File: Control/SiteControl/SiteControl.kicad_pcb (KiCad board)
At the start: 2 copper layers, 109.2 x 48.3 mm, 114 parts, among them J1 RJ50, J2 CONN_01X02, J3 CONN_02X07, J4 CONN_01X06, J5 RS232-Jack, J6 CONN_01X02, J7 USB_A, Q1 BC817-40, Q2 Q_PJFET_GSD, U1 Opto_H11L1M, U10 SS_Relay_VO14642AT, U11 MAX17552, U12 ICL3221, U13 Opto_H11L1M, U14 Opto_H11L1M, U15 12-Bit SPI ADC, U2 Opto_H11L1M, U3 Opto_H11L1M, U4 Opto_H11L1M, U5 Opto_H11L1M, U6 PIC16LF1947, U7 SS_Relay_VO14642AT, U8 SS_Relay_VO14642AT, U9 MC34063, Y1 4MHz

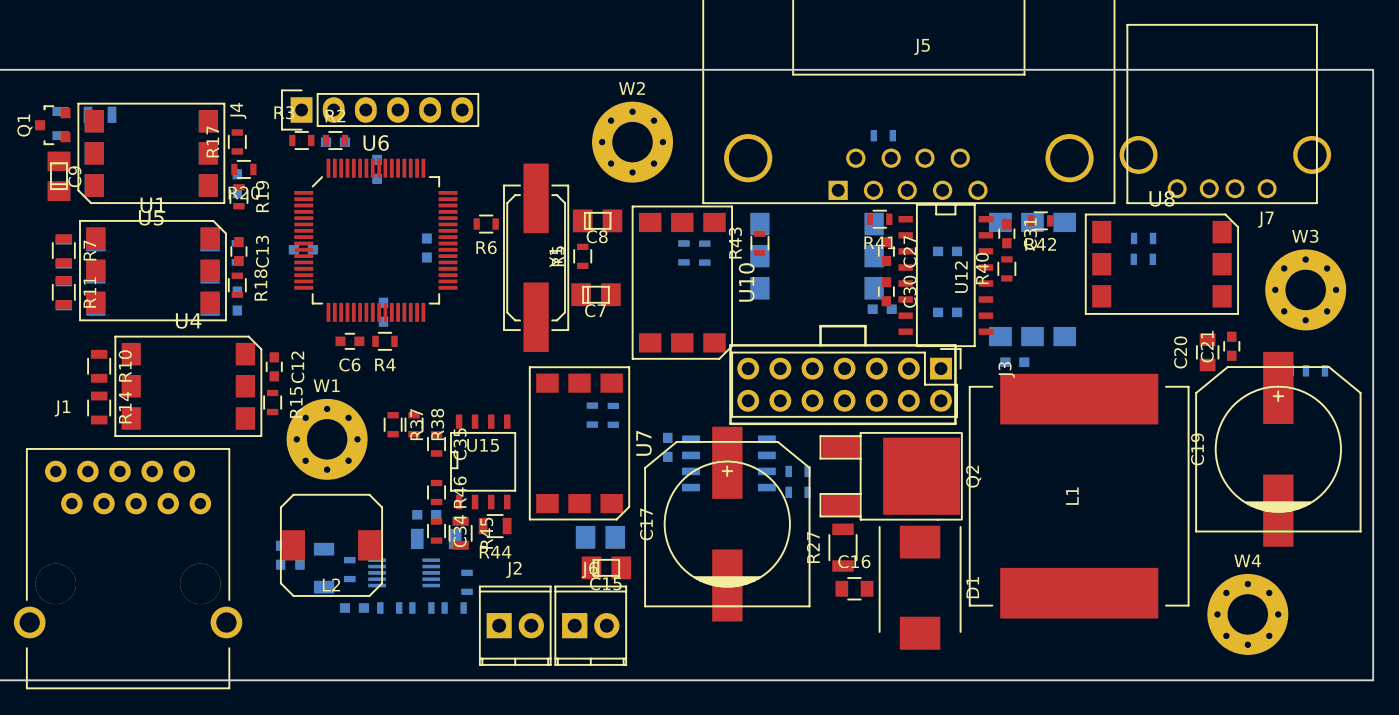
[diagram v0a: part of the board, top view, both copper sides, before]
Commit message: [Changed] Moved mounting holes on control board to positions aligned to 1/16 inch grid
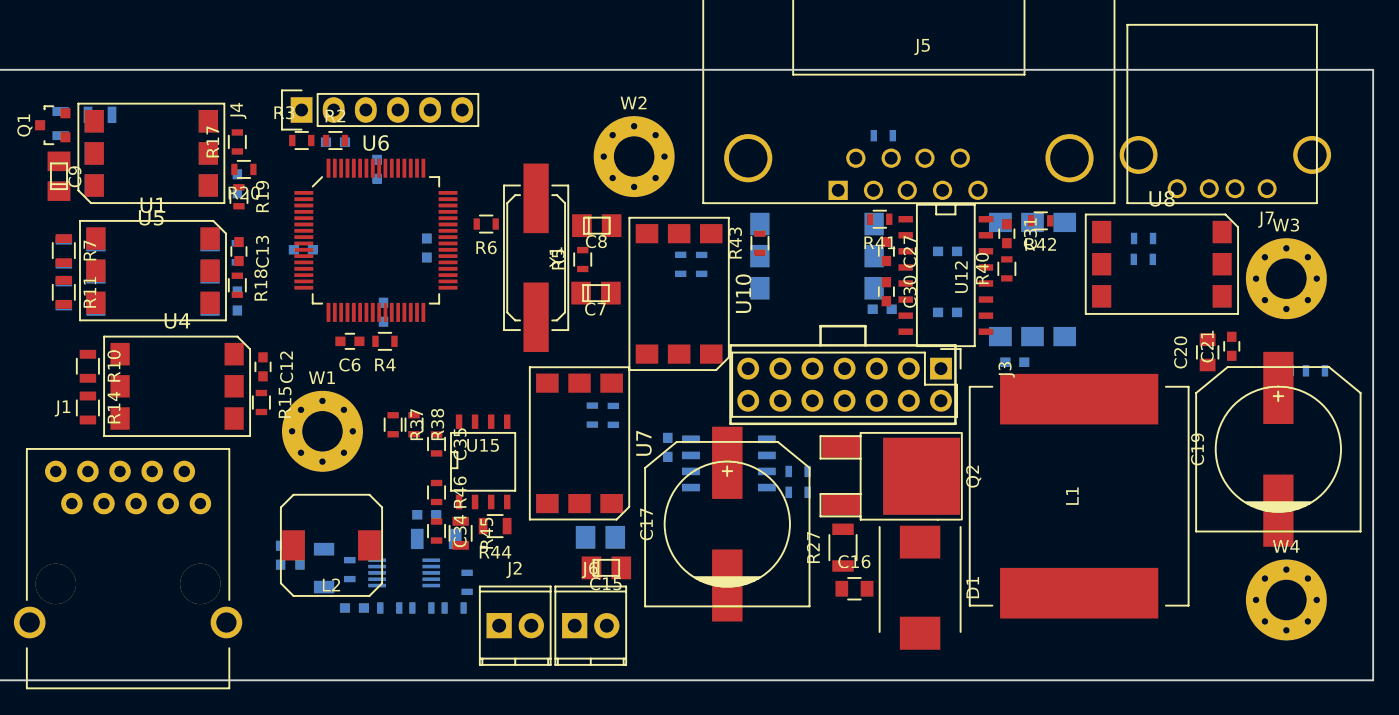
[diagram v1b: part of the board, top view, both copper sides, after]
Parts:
- moved W4 3.26 mm to (188.7, 105.4)
- moved W3 1.76 mm to (188.7, 80.0)
- moved W2 1.15 mm to (137.2, 70.4)
- moved R31 0.92 mm to (140.8, 78.9)
- moved R30 0.92 mm to (142.5, 78.9)
- moved U10 0.92 mm to (140.7, 81.2)
- moved C12 0.89 mm to (107.8, 87.0)
- moved R10 0.89 mm to (94.0, 86.9)
- moved R14 0.89 mm to (94.0, 90.2)
- moved R15 0.89 mm to (107.7, 89.8)
- moved U4 0.89 mm to (101.0, 88.5)
- moved W1 0.73 mm to (112.5, 92.1)
- moved C8 0.39 mm to (134.2, 75.8)
- moved R5 0.25 mm to (133.1, 78.5)
- moved C7 0.13 mm to (134.1, 81.2)
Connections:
- J3 pad 10: CMOS_RTS -> PiSDA
- J3 pad 11: CMOS_RX -> Net-(J3-Pad11)
- J3 pad 12: CMOS_TX -> Pi_VSense
- J3 pad 3: Pi_VSense -> CMOS_TX
- J3 pad 4: Net-(J3-Pad4) -> CMOS_RX
- J3 pad 5: PiSDA -> CMOS_RTS
- J3 pad 6: PiSDA -> CMOS_CTS
- J3 pad 9: CMOS_CTS -> PiSDA
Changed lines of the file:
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@@
     (mod_text_size 1 1)
     (mod_text_width 0.15)
-    (pad_size 1.524 1.524)
-    (pad_drill 0.762)
+    (pad_size 6.4 6.4)
+    (pad_drill 3.2)
     (pad_to_mask_clearance 0.2)
     (aux_axis_origin 0 0)
@@
   (net 115 "Net-(U12-Pad10)")
   (net 116 "Net-(U15-Pad3)")
-  (net 117 "Net-(J4-Pad6)")
-  (net 118 "Net-(J7-Pad3)")
-  (net 119 "Net-(J7-Pad2)")
-  (net 120 "Net-(J7-Pad1)")
-  (net 121 "Net-(J3-Pad4)")
+  (net 117 "Net-(J3-Pad11)")
+  (net 118 "Net-(J4-Pad6)")
+  (net 119 "Net-(J7-Pad3)")
+  (net 120 "Net-(J7-Pad2)")
+  (net 121 "Net-(J7-Pad1)")
   (net_class Default "This is the default net class."
     (clearance 0.2)
@@
     (add_net "Net-(C8-Pad1)")
     (add_net "Net-(D1-Pad1)")
-    (add_net "Net-(J3-Pad4)")
+    (add_net "Net-(J3-Pad11)")
     (add_net "Net-(J4-Pad6)")
     (add_net "Net-(J7-Pad1)")
@@
   )
   (module Capacitors_Tantalum_SMD:TantalC_SizeR_EIA-2012 (layer F.Cu)
-    (at 134.14502 81.28 180)
+    (at 134.14502 81.153 180)
     (descr "Tantal Cap. , Size C, EIA-2012")
     (fp_text reference C7 (at 0.0254 -1.2954 180) (layer F.SilkS)
@@
   )
   (module Capacitors_Tantalum_SMD:TantalC_SizeR_EIA-2012 (layer F.Cu)
-    (at 134.27202 75.438 180)
+    (at 134.20598 75.819 180)
     (descr "Tantal Cap. , Size C, EIA-2012")
     (fp_text reference C8 (at 0.0254 -1.2954 180) (layer F.SilkS)
@@
   )
   (module Resistors_SMD:R_0603 (layer F.Cu)
-    (at 133.096 78.244 90)
+    (at 133.096 78.498 90)
     (descr "Resistor SMD 0603, reflow soldering, Vishay (see dcrcw.pdf)")
     (tags "resistor 0603")
@@
   )
   (module Capacitors_SMD:C_0603 (layer F.Cu)
-    (at 108.712 86.983 270)
+    (at 107.823 86.983 270)
     (descr "Capacitor SMD 0603, reflow soldering, AVX (see smccp.pdf)")
     (tags "capacitor 0603")
@@
   )
   (module Resistors_SMD:R_0805 (layer F.Cu)
-    (at 94.869 86.934 270)
+    (at 93.98 86.934 270)
     (descr "Resistor SMD 0805, reflow soldering, Vishay (see dcrcw.pdf)")
     (tags "resistor 0805")
@@
   )
   (module Resistors_SMD:R_0805 (layer F.Cu)
-    (at 94.869 90.231 270)
+    (at 93.98 90.231 270)
     (descr "Resistor SMD 0805, reflow soldering, Vishay (see dcrcw.pdf)")
     (tags "resistor 0805")
@@
   )
   (module Resistors_SMD:R_0603 (layer F.Cu)
-    (at 108.585 89.801 270)
+    (at 107.696 89.801 270)
     (descr "Resistor SMD 0603, reflow soldering, Vishay (see dcrcw.pdf)")
     (tags "resistor 0603")
@@
   )
   (module Resistors_SMD:R_0603 (layer B.Cu)
-    (at 142.748 77.99 90)
+    (at 142.494 78.879 90)
     (descr "Resistor SMD 0603, reflow soldering, Vishay (see dcrcw.pdf)")
     (tags "resistor 0603")
@@
   )
   (module Resistors_SMD:R_0603 (layer B.Cu)
-    (at 141.097 77.978 90)
+    (at 140.843 78.867 90)
     (descr "Resistor SMD 0603, reflow soldering, Vishay (see dcrcw.pdf)")
     (tags "resistor 0603")
@@
   )
   (module Mounting_Holes:MountingHole_3.2mm_M3_Pad_Via (layer F.Cu)
-    (at 112.89 92.71)
+    (at 112.522 92.075)
     (descr "Mounting Hole 3.2mm, M3")
     (tags "mounting hole 3.2mm m3")
@@
   )
   (module Mounting_Holes:MountingHole_3.2mm_M3_Pad_Via (layer F.Cu)
-    (at 137.033 69.215)
+    (at 137.16 70.358)
     (descr "Mounting Hole 3.2mm, M3")
     (tags "mounting hole 3.2mm m3")
@@
   )
   (module Mounting_Holes:MountingHole_3.2mm_M3_Pad_Via (layer F.Cu)
-    (at 190.246 80.899)
+    (at 188.722 80.01)
     (descr "Mounting Hole 3.2mm, M3")
     (tags "mounting hole 3.2mm m3")
@@
   )
   (module Mounting_Holes:MountingHole_3.2mm_M3_Pad_Via (layer F.Cu)
-    (at 185.674 106.553)
+    (at 188.722 105.41)
     (descr "Mounting Hole 3.2mm, M3")
     (tags "mounting hole 3.2mm m3")
@@
   )
   (module DigitalLogic:H11L1M (layer F.Cu)
-    (at 101.919 88.519 270)
+    (at 101.03 88.519 270)
     (fp_text reference U4 (at -5.13 0 360) (layer F.SilkS)
       (effects (font (size 1.2 1.2) (thickness 0.15)))
@@
   )
   (module DigitalLogic:SS_Relay_VO14642AT (layer F.Cu)
-    (at 140.97 80.325 180)
+    (at 140.716 81.214 180)
     (fp_text reference U10 (at -5.13 0 270) (layer F.SilkS)
       (effects (font (size 1.2 1.2) (thickness 0.15)))
@@
       (net 10 RPi_En))
     (pad 5 smd rect (at 0 -4.76 270) (size 1.78 1.52) (layers F.Cu F.Paste F.Mask)
-      (net 120 "Net-(J7-Pad1)"))
+      (net 121 "Net-(J7-Pad1)"))
     (pad 2 smd rect (at 0 4.76 270) (size 1.78 1.52) (layers F.Cu F.Paste F.Mask)
       (net 79 "Net-(R23-Pad2)"))
@@
       (net 2 GND))
     (pad 3 thru_hole oval (at 0 2.54 270) (size 1.7272 1.7272) (drill 1.016) (layers *.Cu *.Mask F.SilkS)
-      (net 35 Pi_VSense))
+      (net 13 CMOS_TX))
     (pad 4 thru_hole oval (at 2.54 2.54 270) (size 1.7272 1.7272) (drill 1.016) (layers *.Cu *.Mask F.SilkS)
-      (net 121 "Net-(J3-Pad4)"))
+      (net 14 CMOS_RX))
     (pad 5 thru_hole oval (at 0 5.08 270) (size 1.7272 1.7272) (drill 1.016) (layers *.Cu *.Mask F.SilkS)
-      (net 37 PiSDA))
+      (net 32 CMOS_RTS))
     (pad 6 thru_hole oval (at 2.54 5.08 270) (size 1.7272 1.7272) (drill 1.016) (layers *.Cu *.Mask F.SilkS)
-      (net 37 PiSDA))
+      (net 31 CMOS_CTS))
     (pad 7 thru_hole oval (at 0 7.62 270) (size 1.7272 1.7272) (drill 1.016) (layers *.Cu *.Mask F.SilkS)
       (net 36 PiSCL))
@@
       (net 36 PiSCL))
     (pad 9 thru_hole oval (at 0 10.16 270) (size 1.7272 1.7272) (drill 1.016) (layers *.Cu *.Mask F.SilkS)
-      (net 31 CMOS_CTS))
+      (net 37 PiSDA))
     (pad 10 thru_hole oval (at 2.54 10.16 270) (size 1.7272 1.7272) (drill 1.016) (layers *.Cu *.Mask F.SilkS)
-      (net 32 CMOS_RTS))
+      (net 37 PiSDA))
     (pad 11 thru_hole oval (at 0 12.7 270) (size 1.7272 1.7272) (drill 1.016) (layers *.Cu *.Mask F.SilkS)
-      (net 14 CMOS_RX))
+      (net 117 "Net-(J3-Pad11)"))
     (pad 12 thru_hole oval (at 2.54 12.7 270) (size 1.7272 1.7272) (drill 1.016) (layers *.Cu *.Mask F.SilkS)
-      (net 13 CMOS_TX))
+      (net 35 Pi_VSense))
     (pad 13 thru_hole oval (at 0 15.24 270) (size 1.7272 1.7272) (drill 1.016) (layers *.Cu *.Mask F.SilkS)
       (net 2 GND))
@@
       (net 40 PGEC))
     (pad 6 thru_hole oval (at 0 12.7 90) (size 2.032 1.7272) (drill 1.016) (layers *.Cu *.Mask F.SilkS)
-      (net 117 "Net-(J4-Pad6)"))
+      (net 118 "Net-(J4-Pad6)"))
     (model Pin_Headers.3dshapes/Pin_Header_Straight_1x06.wrl
       (at (xyz 0 -0.25 0))
@@
       (net 2 GND))
     (pad 3 thru_hole circle (at 4.57286 -0.00212 90) (size 1.50114 1.50114) (drill 1.00076) (layers *.Cu *.Mask F.SilkS)
-      (net 118 "Net-(J7-Pad3)"))
+      (net 119 "Net-(J7-Pad3)"))
     (pad 2 thru_hole circle (at 2.54086 -0.00212 90) (size 1.50114 1.50114) (drill 1.00076) (layers *.Cu *.Mask F.SilkS)
-      (net 119 "Net-(J7-Pad2)"))
+      (net 120 "Net-(J7-Pad2)"))
     (pad 1 thru_hole circle (at 0.00086 -0.00212 90) (size 1.50114 1.50114) (drill 1.00076) (layers *.Cu *.Mask F.SilkS)
-      (net 120 "Net-(J7-Pad1)"))
+      (net 121 "Net-(J7-Pad1)"))
     (pad 5 thru_hole circle (at 10.16086 2.66488 90) (size 2.99974 2.99974) (drill 2.30124) (layers *.Cu *.Mask F.SilkS)
       (net 2 GND))

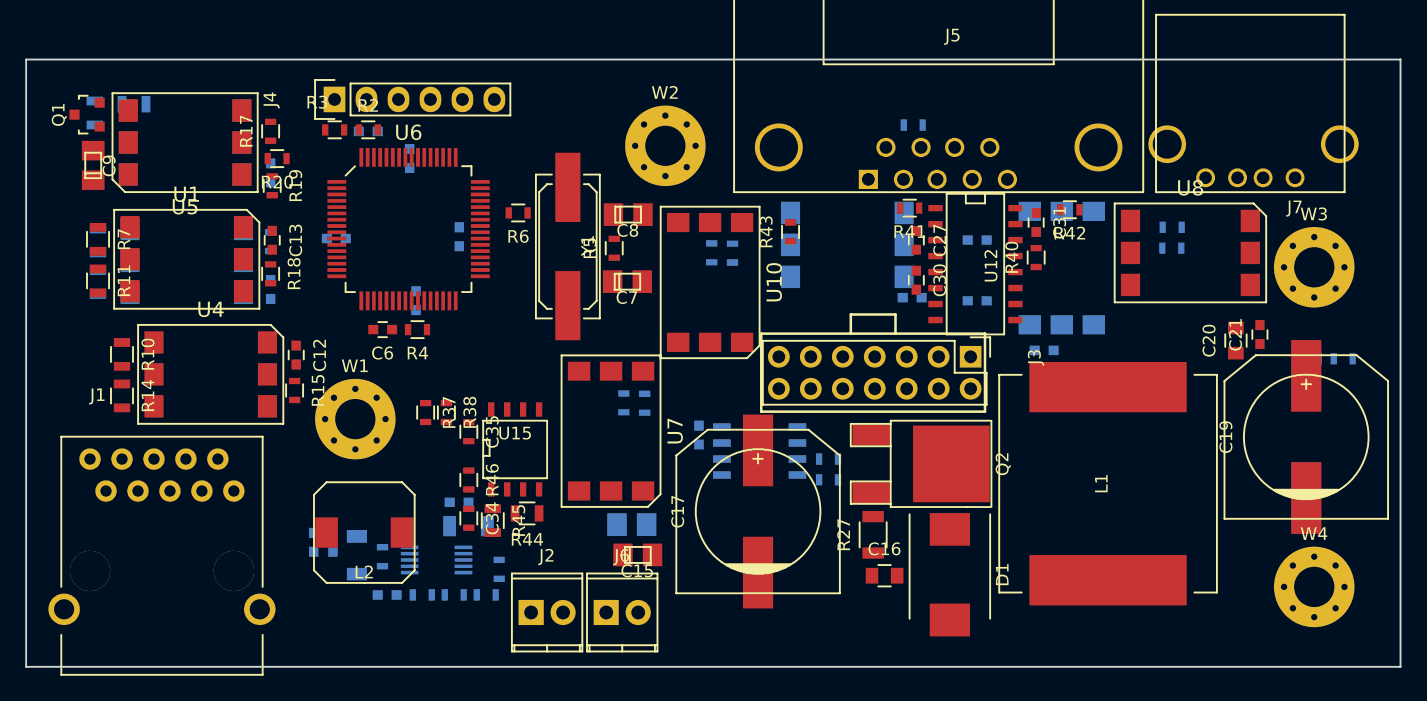
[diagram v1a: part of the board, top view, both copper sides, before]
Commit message: [Completed] Layout of controller board (passed DRC) - still needs silkscreen fix
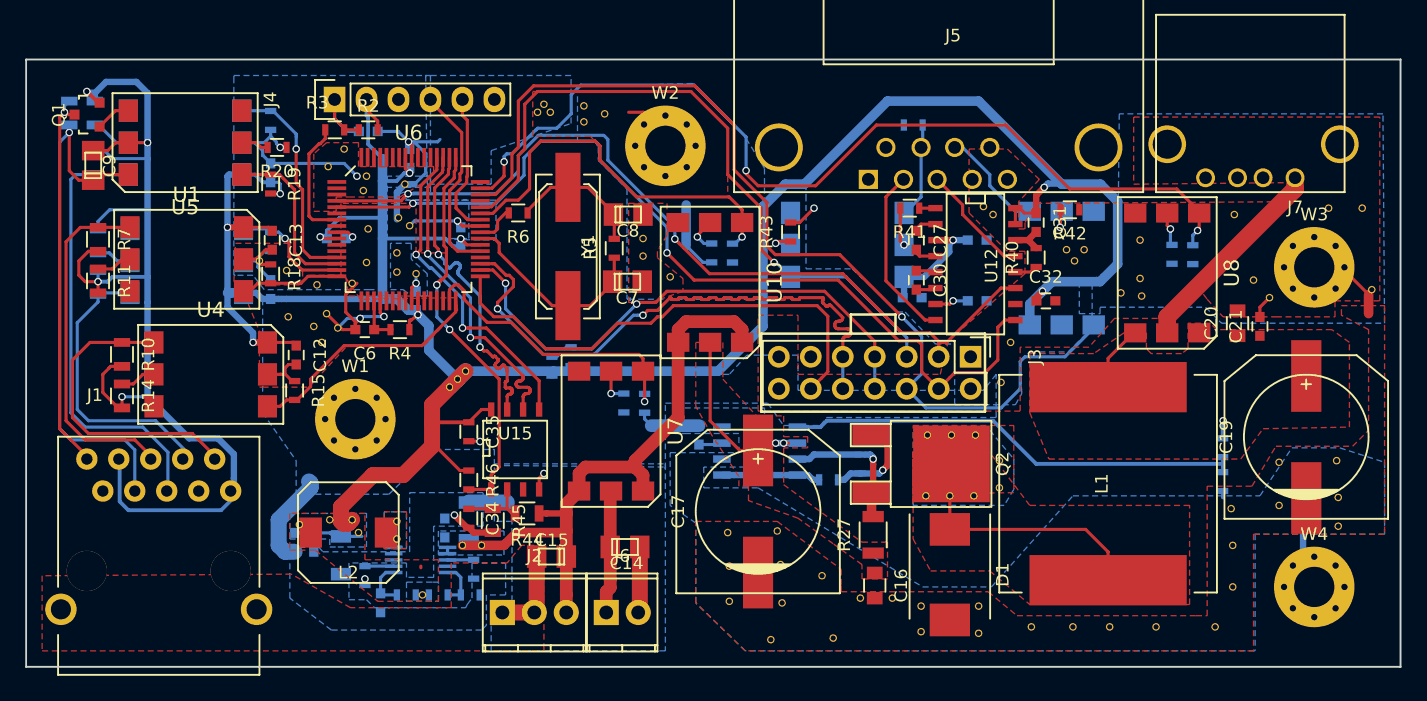
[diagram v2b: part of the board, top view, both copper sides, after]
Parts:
- added ?: , DigitalLogic:Via, F.Cu at (107.1, 80.3)
- added ?: , DigitalLogic:Via, F.Cu at (175.0, 82.3)
- added ?: , DigitalLogic:Via, F.Cu at (174.9, 80.9)
- added ?: , DigitalLogic:Via, F.Cu at (173.4, 82.0)
- added ?: , DigitalLogic:Via, F.Cu at (169.7, 79.5)
- added ?: , DigitalLogic:Via, F.Cu at (170.4, 78.6)
- added ?: , DigitalLogic:Via, F.Cu at (169.0, 78.6)
- added ?: , DigitalLogic:Via, F.Cu at (163.2, 75.8)
- added ?: , DigitalLogic:Via, F.Cu at (162.4, 75.2)
- added ?: , DigitalLogic:Via, F.Cu at (164.6, 86.0)
- added ?: , DigitalLogic:Via, F.Cu at (163.8, 89.2)
- added ?: , DigitalLogic:Via, F.Cu at (104.9, 79.5)
- added ?: , DigitalLogic:Via, F.Cu at (137.5, 80.8)
- added ?: , DigitalLogic:Via, F.Cu at (135.4, 79.1)
- added ?: , DigitalLogic:Via, F.Cu at (135.4, 77.7)
- added ?: , DigitalLogic:Via, F.Cu at (132.3, 67.8)
- added ?: , DigitalLogic:Via, F.Cu at (130.7, 67.2)
- added ?: , DigitalLogic:Via, F.Cu at (130.7, 68.5)
- added ?: , DigitalLogic:Via, F.Cu at (128.0, 67.7)
- added ?: , DigitalLogic:Via, F.Cu at (127.0, 67.7)
- added ?: , DigitalLogic:Via, F.Cu at (127.5, 67.1)
- added ?: , DigitalLogic:Via, F.Cu at (110.4, 72.0)
- added ?: , DigitalLogic:Via, F.Cu at (193.3, 81.8)
- added ?: , DigitalLogic:Via, F.Cu at (111.6, 70.6)
- added ?: , DigitalLogic:Via, F.Cu at (116.5, 73.4)
- added ?: , DigitalLogic:Via, F.Cu at (113.4, 72.8)
- added ?: , DigitalLogic:Via, F.Cu at (113.2, 73.9)
- added ?: , DigitalLogic:Via, F.Cu at (117.3, 80.5)
- added ?: , DigitalLogic:Via, F.Cu at (115.8, 80.4)
- added ?: , DigitalLogic:Via, F.Cu at (115.8, 78.9)
- added ?: , DigitalLogic:Via, F.Cu at (116.8, 76.7)
- added ?: , DigitalLogic:Via, F.Cu at (116.0, 76.1)
- added ?: , DigitalLogic:Via, F.Cu at (113.5, 77.0)
- added ?: , DigitalLogic:Via, F.Cu at (192.5, 75.3)
- added ?: , DigitalLogic:Via, F.Cu at (113.4, 79.6)
- added ?: , DigitalLogic:Via, F.Cu at (112.3, 81.3)
- added ?: , DigitalLogic:Via, F.Cu at (109.5, 81.4)
- added ?: , DigitalLogic:Via, F.Cu at (110.2, 83.7)
- added ?: , DigitalLogic:Via, F.Cu at (107.2, 83.9)
- added ?: , DigitalLogic:Via, F.Cu at (109.2, 84.7)
- added ?: , DigitalLogic:Via, F.Cu at (111.1, 84.8)
- added ?: , DigitalLogic:Via, F.Cu at (109.9, 86.0)
- added ?: , DigitalLogic:Via, F.Cu at (120.0, 89.5)
- added ?: , DigitalLogic:Via, F.Cu at (120.7, 88.9)
- added ?: , DigitalLogic:Via, F.Cu at (189.9, 75.3)
- added ?: , DigitalLogic:Via, F.Cu at (121.3, 88.3)
- added ?: , DigitalLogic:Via, F.Cu at (149.6, 104.5)
- added ?: , DigitalLogic:Via, F.Cu at (145.5, 109.6)
- added ?: , DigitalLogic:Via, F.Cu at (150.5, 109.5)
- added ?: , DigitalLogic:Via, F.Cu at (190.6, 100.6)
- added ?: , DigitalLogic:Via, F.Cu at (190.6, 98.3)
- added ?: , DigitalLogic:Via, F.Cu at (190.5, 95.4)
- added ?: , DigitalLogic:Via, F.Cu at (185.9, 95.5)
- added ?: , DigitalLogic:Via, F.Cu at (185.9, 98.9)
- added ?: , DigitalLogic:Via, F.Cu at (182.1, 99.2)
- added ?: , DigitalLogic:Via, F.Cu at (185.2, 82.4)
- added ?: , DigitalLogic:Via, F.Cu at (182.2, 102.1)
- added ?: , DigitalLogic:Via, F.Cu at (182.2, 105.4)
- added ?: , DigitalLogic:Via, F.Cu at (180.8, 108.6)
- added ?: , DigitalLogic:Via, F.Cu at (176.1, 108.6)
- added ?: , DigitalLogic:Via, F.Cu at (172.5, 108.6)
- added ?: , DigitalLogic:Via, F.Cu at (169.5, 108.6)
- added ?: , DigitalLogic:Via, F.Cu at (166.2, 108.6)
- added ?: , DigitalLogic:Via, F.Cu at (157.5, 109.0)
- added ?: , DigitalLogic:Via, F.Cu at (162.1, 109.1)
- added ?: , DigitalLogic:Via, F.Cu at (162.1, 106.9)
- added ?: , DigitalLogic:Via, F.Cu at (183.9, 81.0)
- added ?: , DigitalLogic:Via, F.Cu at (157.5, 106.9)
- added ?: , DigitalLogic:Via, F.Cu at (155.2, 106.3)
- added ?: , DigitalLogic:Via, F.Cu at (152.7, 106.3)
- added ?: , DigitalLogic:Via, F.Cu at (146.4, 106.7)
- added ?: , DigitalLogic:Via, F.Cu at (142.2, 106.6)
- added ?: , DigitalLogic:Via, F.Cu at (142.2, 103.8)
- added ?: , DigitalLogic:Via, F.Cu at (146.3, 103.6)
- added ?: , DigitalLogic:Via, F.Cu at (146.1, 101.0)
- added ?: , DigitalLogic:Via, F.Cu at (142.1, 101.1)
- added ?: , DigitalLogic:Via, F.Cu at (159.9, 93.3)
- added ?: , DigitalLogic:Via, F.Cu at (182.4, 75.8)
- added ?: , DigitalLogic:Via, F.Cu at (158.0, 93.3)
- added ?: , DigitalLogic:Via, F.Cu at (161.8, 93.3)
- added ?: , DigitalLogic:Via, F.Cu at (163.7, 95.4)
- added ?: , DigitalLogic:Via, F.Cu at (163.7, 97.5)
- added ?: , DigitalLogic:Via, F.Cu at (161.7, 98.2)
- added ?: , DigitalLogic:Via, F.Cu at (159.8, 98.2)
- added ?: , DigitalLogic:Via, F.Cu at (157.9, 98.2)
- added ?: , DigitalLogic:Via, F.Cu at (122.6, 102.1)
- added ?: , DigitalLogic:Via, F.Cu at (121.0, 102.1)
- added ?: , DigitalLogic:Via, F.Cu at (117.9, 106.0)
- added ?: , DigitalLogic:Via, F.Cu at (174.9, 77.9)
- added ?: , DigitalLogic:Via, F.Cu at (108.1, 100.5)
- added ?: , DigitalLogic:Via, F.Cu at (112.8, 101.1)
- added ?: , DigitalLogic:Via, F.Cu at (110.5, 100.1)
- added ?: , DigitalLogic:Via, F.Cu at (112.3, 100.1)
- added ?: , DigitalLogic:Via, F.Cu at (115.8, 100.2)
- added ?: , DigitalLogic:Via, F.Cu at (115.8, 101.6)
- C14, C32: moved to F.Cu
- J2: value CONN_01X02 -> CONN_01X03; footprint Terminal_Blocks:TerminalBlock_Pheonix_MPT-2.54mm_2pol -> Terminal_Blocks:TerminalBlock_Pheonix_MPT-2.54mm_3pol
- R17, R37, R38: moved to B.Cu
- moved R29 13.7 mm to (181.4, 97.0), turned to 270 degrees
- moved R37 12.4 mm to (129.7, 87.1)
- moved R28 9.86 mm to (181.4, 94.3), turned to 270 degrees
- moved R38 9.16 mm to (128.1, 87.9)
- moved C15 6.86 mm to (128.1, 103.0), turned to 0 degrees
- moved R8 5.66 mm to (91.7, 71.7), turned to 90 degrees
- moved R1 4.60 mm to (89.8, 67.8)
- moved C32 3.94 mm to (167.4, 82.7)
- moved C25 3.05 mm to (107.7, 101.9)
- moved R24 2.72 mm to (179.1, 79.0), turned to 90 degrees
- moved R25 2.56 mm to (152.7, 95.6), turned to 270 degrees
- moved U8 2.43 mm to (177.0, 80.5), turned to 180 degrees
- moved C36 2.34 mm to (119.6, 100.7), turned to 90 degrees
- moved J2 2.29 mm to (124.2, 107.4)
- moved R36 2.05 mm to (113.3, 104.5), turned to 270 degrees
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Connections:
- J2 pad 2: +BATT -> GND
- R30 pad 2: RPi_5v_En -> RPi_5V_En
- U10 pad 1: RPi_5v_En -> RPi_5V_En
- U6 pad 1: RPi_En -> Net-(U6-Pad1)
- U6 pad 13: Net-(U6-Pad13) -> INV_Power_Safe
- U6 pad 14: Net-(U6-Pad14) -> INV_Toggle_Safe
- U6 pad 15: Net-(U6-Pad15) -> INV_Overload_Safe
- U6 pad 16: Net-(U6-Pad16) -> INV_Temp_Safe
- U6 pad 21: INV_Toggle_Safe -> Net-(U6-Pad21)
- U6 pad 22: INV_Temp_Safe -> Net-(U6-Pad22)
- U6 pad 23: INV_Power_Safe -> Net-(U6-Pad23)
- U6 pad 24: INV_Overload_Safe -> Net-(U6-Pad24)
- U6 pad 29: CMOS_CTS -> Net-(U6-Pad29)
- U6 pad 30: CMOS_RTS -> Net-(U6-Pad30)
- U6 pad 31: Net-(U6-Pad31) -> Modem_En
- U6 pad 43: Net-(U6-Pad43) -> RPi_5V_En
- U6 pad 44: Net-(U6-Pad44) -> CMOS_RTS
- U6 pad 46: Net-(U6-Pad46) -> CMOS_CTS
- U6 pad 47: Net-(U6-Pad47) -> RPi_En
- U6 pad 64: Modem_En -> Net-(U6-Pad64)
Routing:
- net +3V3: track 0.00 -> 221.5 mm, vias 0 -> 10
- net GND: track 0.00 -> 137.6 mm, vias 0 -> 13
- net INV_LCD_GND: track 0.00 -> 90.0 mm, vias 0 -> 4
- net CMOS_CTS: track 0.00 -> 78.6 mm, vias 0 -> 1
- net RPi_En: track 0.00 -> 75.1 mm, vias 0 -> 3
- net CMOS_RX: track 0.00 -> 72.0 mm, vias 0 -> 2
- net CMOS_TX: track 0.00 -> 69.3 mm, vias 0 -> 2
- net CMOS_RTS: track 0.00 -> 54.6 mm, vias 0 -> 1
- net +BATT: track 0.00 -> 48.6 mm
- net PiSDA: track 0.00 -> 47.0 mm, vias 0 -> 2
- net INV_VCC: track 0.00 -> 42.7 mm, vias 0 -> 1
- net PiSCL: track 0.00 -> 42.6 mm, vias 0 -> 2
- net Pi_VSense: track 0.00 -> 39.3 mm
- net Net-(R28-Pad2): track 0.00 -> 36.6 mm
- net INV_LED_OverTemp: track 0.00 -> 35.4 mm
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- added copper zone on B.Cu, net +3V3
- added copper zone on F.Cu, net +3V3
- added copper zone on F.Cu, net +5V
- added copper zone on B.Cu, net +BATT
- added copper zone on B.Cu, net GND
- added copper zone on F.Cu, net GND
- added copper zone on F.Cu, net Net-(C16-Pad1)
- added copper zone on B.Cu, net Net-(D1-Pad1)
- added copper zone on F.Cu, net Net-(D1-Pad1)
- added copper zone on B.Cu, net Net-(L2-Pad1)
- added copper zone on F.Cu, net Net-(L2-Pad1)
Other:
- rule trace_min: 0.2 -> 0.1524
